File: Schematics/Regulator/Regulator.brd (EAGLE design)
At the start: 42.9 x 68.6 mm, 28 parts, among them IC1 LM317BD2T, IC2 LM337_D2PAC

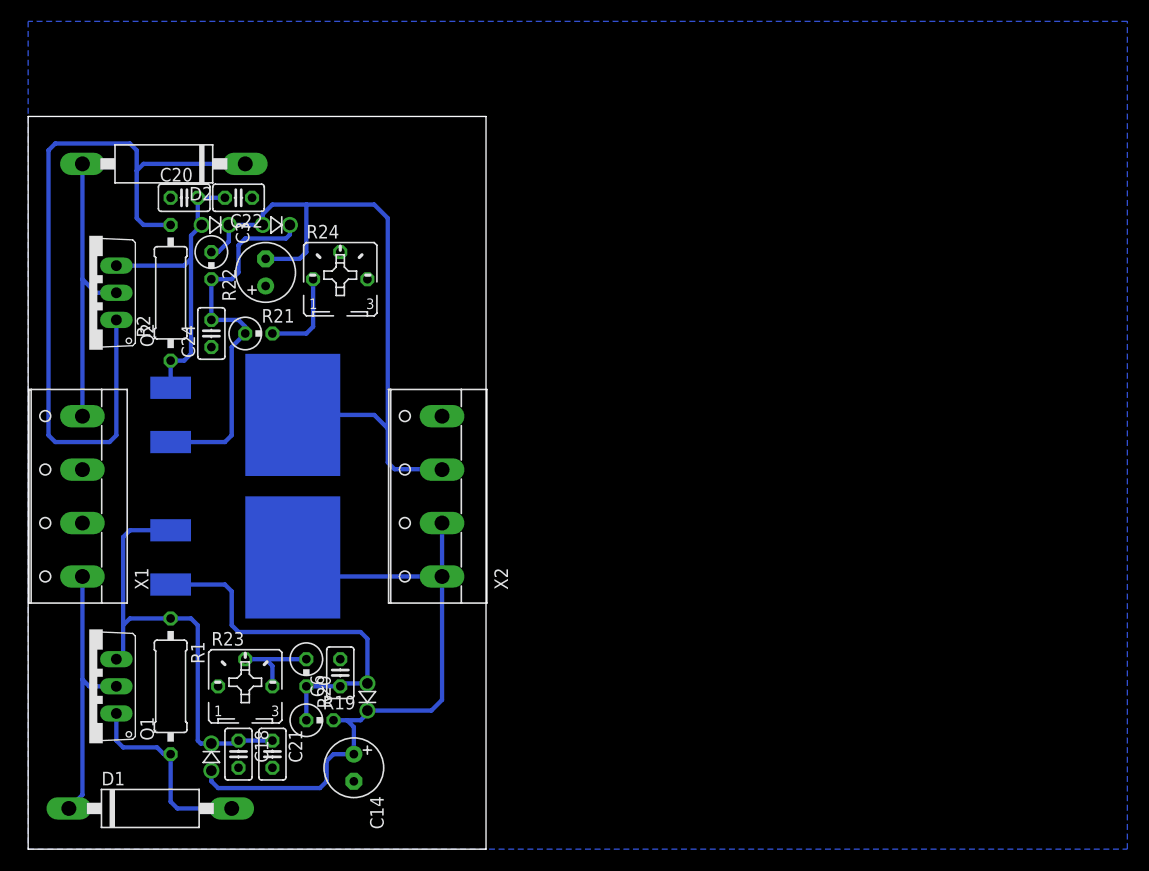
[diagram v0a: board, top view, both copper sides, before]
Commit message: updated gerbers for regulator board
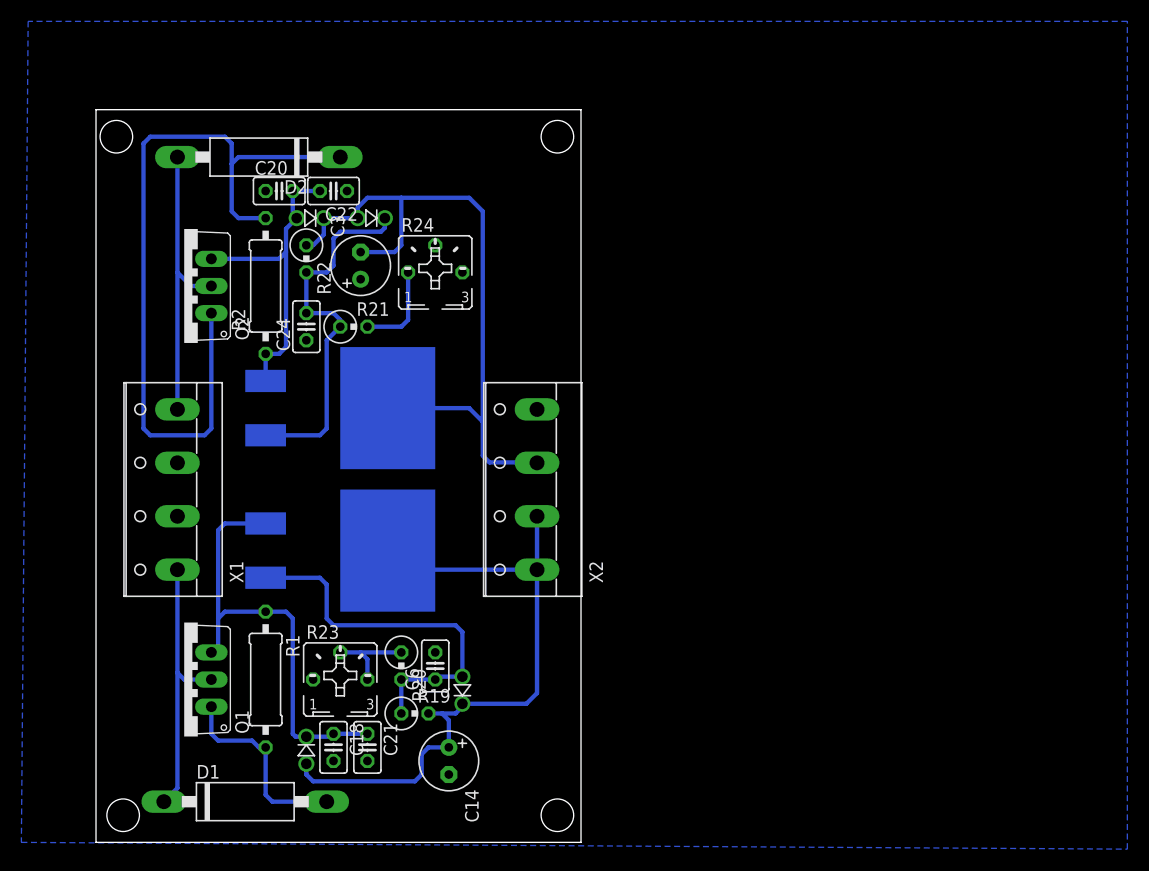
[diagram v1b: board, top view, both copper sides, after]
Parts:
- C24, C6: value 10uF -> 0.1uF
- moved C18 8.91 mm to (28.6, 9.53)
- moved C20 8.91 mm to (23.5, 61.6)
- moved C21 8.91 mm to (31.8, 9.53)
- moved C22 8.91 mm to (28.6, 61.6)
- moved C24 8.91 mm to (26.0, 48.9)
- moved C6 8.91 mm to (38.1, 17.1)
- moved D1 8.91 mm to (20.3, 4.45)
- moved D11 8.91 mm to (26.0, 12.1)
- moved D12 8.91 mm to (40.6, 12.1)
- moved D18 8.91 mm to (29.2, 59.1)
- moved D2 8.91 mm to (21.6, 64.8)
- moved Q1 8.91 mm to (14.6, 15.9)
- moved Q2 8.91 mm to (14.6, 52.7)
- moved R1 8.91 mm to (22.2, 15.9)
- moved R19 8.91 mm to (36.2, 12.7)
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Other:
- board size 42.9 x 68.6 mm -> 45.4 x 68.6 mm
